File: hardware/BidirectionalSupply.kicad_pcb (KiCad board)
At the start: 4 copper layers, 132 x 107 mm, 190 parts, among them J1 USB-309GC-B-SU, J10 Conn_01x02, J11 Conn_01x08, J12 Conn_01x05, J13 Conn_01x02, J2 CON10, J3 CON2, J6 CON4, J7 CON2, J8 Conn_01x03, J9 Conn_01x12, Q1 SIR880BDP, Q10 SIR880BDP, Q11 SIR880BDP, Q12 SIR880BDP, Q2 SIR880BDP, Q3 SIR880BDP, Q4 SIR880BDP, Q5 SIR880BDP, Q6 SIR880BDP, Q7 SIR880BDP, Q8 SIR880BDP, Q9 SIR880BDP, SW1 SW_Push, SW2 SW_Push, U1 W25Q128JVS, U2 LM74810QDRRRQ1, U3 RP2350_60QFN, U4 BQ25758, U5 MAX17502EATB+T, U6 LM74810QDRRRQ1, U7 LM74810QDRRRQ1, U8 LM74810QDRRRQ1, Y1 ABM8-272-T3

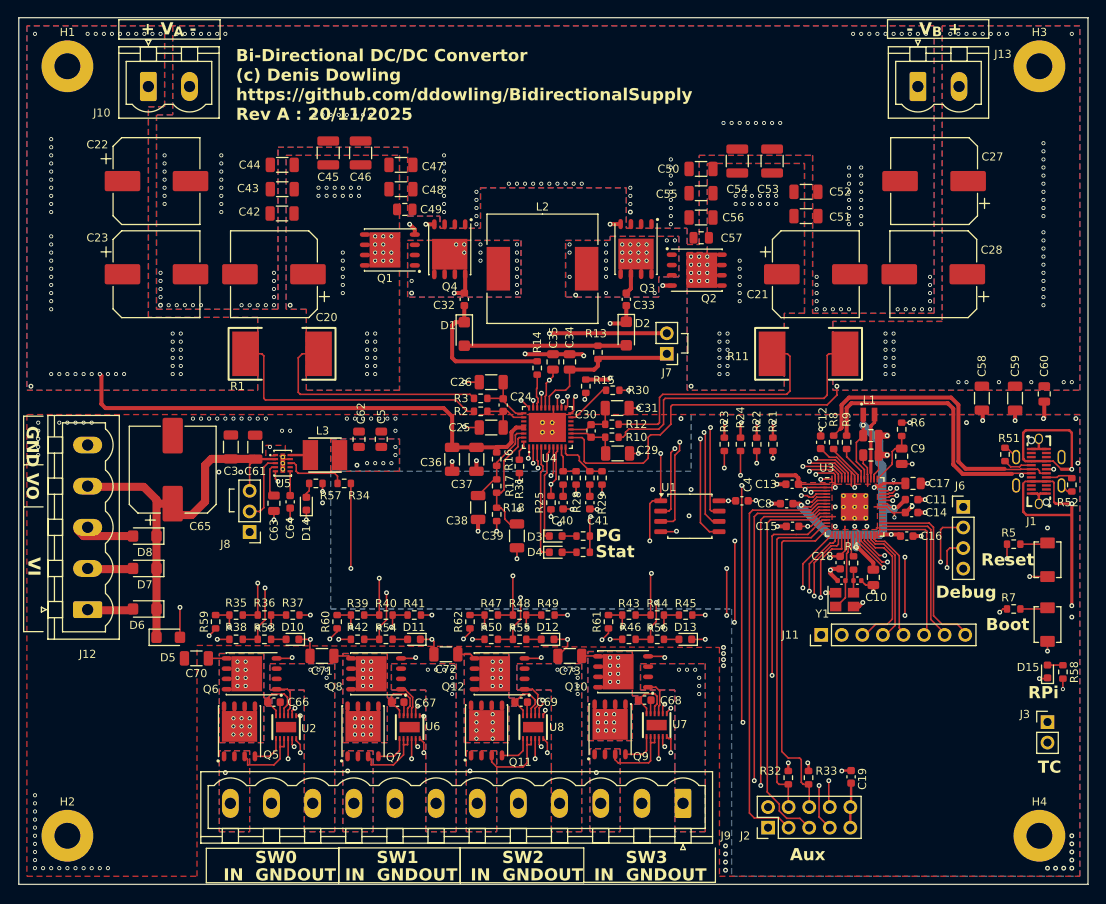
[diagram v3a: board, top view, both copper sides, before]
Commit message: * Added the JLCPCB Fabrication Plugin into KiCad and use this for the exports * Fixed problem detected with capacitor footprint for C42, C43, C44, C50, C51, C52
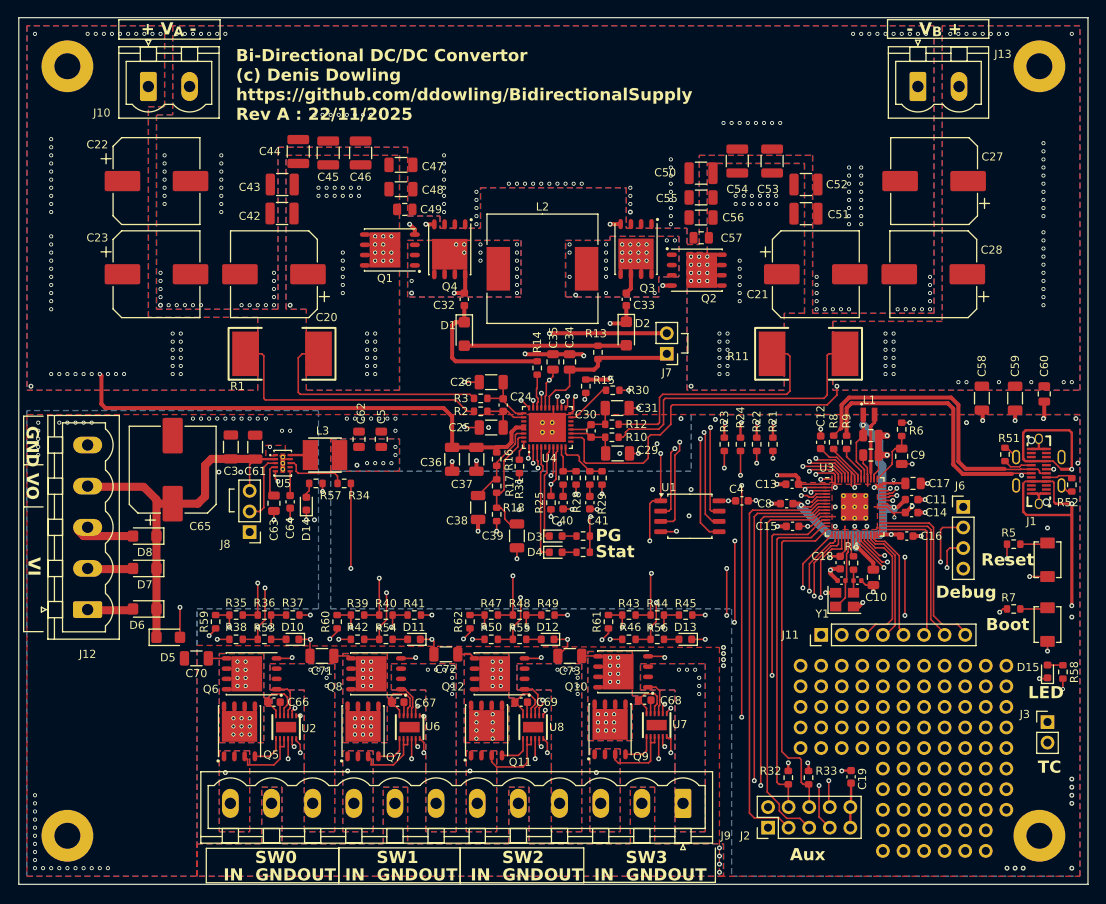
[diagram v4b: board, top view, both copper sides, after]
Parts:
- added REF**: Pad_D1.7mm_Drill1.0mm, BidirectionalSupply:Pad_D1.7mm_Drill1.0mm, F.Cu at (166.8, 132.6)
- added REF**: Pad_D1.7mm_Drill1.0mm, BidirectionalSupply:Pad_D1.7mm_Drill1.0mm, F.Cu at (151.6, 140.2)
- added REF**: Pad_D1.7mm_Drill1.0mm, BidirectionalSupply:Pad_D1.7mm_Drill1.0mm, F.Cu at (149.1, 140.2)
- added REF**: Pad_D1.7mm_Drill1.0mm, BidirectionalSupply:Pad_D1.7mm_Drill1.0mm, F.Cu at (171.9, 130.0)
- added REF**: Pad_D1.7mm_Drill1.0mm, BidirectionalSupply:Pad_D1.7mm_Drill1.0mm, F.Cu at (169.4, 132.6)
- added REF**: Pad_D1.7mm_Drill1.0mm, BidirectionalSupply:Pad_D1.7mm_Drill1.0mm, F.Cu at (156.7, 152.9)
- added REF**: Pad_D1.7mm_Drill1.0mm, BidirectionalSupply:Pad_D1.7mm_Drill1.0mm, F.Cu at (151.6, 132.6)
- added REF**: Pad_D1.7mm_Drill1.0mm, BidirectionalSupply:Pad_D1.7mm_Drill1.0mm, F.Cu at (156.7, 145.2)
- added REF**: Pad_D1.7mm_Drill1.0mm, BidirectionalSupply:Pad_D1.7mm_Drill1.0mm, F.Cu at (149.1, 132.6)
- added REF**: Pad_D1.7mm_Drill1.0mm, BidirectionalSupply:Pad_D1.7mm_Drill1.0mm, F.Cu at (161.8, 130.0)
- added REF**: Pad_D1.7mm_Drill1.0mm, BidirectionalSupply:Pad_D1.7mm_Drill1.0mm, F.Cu at (149.1, 130.0)
- added REF**: Pad_D1.7mm_Drill1.0mm, BidirectionalSupply:Pad_D1.7mm_Drill1.0mm, F.Cu at (166.8, 147.8)
- added REF**: Pad_D1.7mm_Drill1.0mm, BidirectionalSupply:Pad_D1.7mm_Drill1.0mm, F.Cu at (164.3, 132.6)
- added REF**: Pad_D1.7mm_Drill1.0mm, BidirectionalSupply:Pad_D1.7mm_Drill1.0mm, F.Cu at (146.5, 140.2)
- added REF**: Pad_D1.7mm_Drill1.0mm, BidirectionalSupply:Pad_D1.7mm_Drill1.0mm, F.Cu at (159.2, 135.1)
- added REF**: Pad_D1.7mm_Drill1.0mm, BidirectionalSupply:Pad_D1.7mm_Drill1.0mm, F.Cu at (166.8, 152.9)
- added REF**: Pad_D1.7mm_Drill1.0mm, BidirectionalSupply:Pad_D1.7mm_Drill1.0mm, F.Cu at (151.6, 130.0)
- added REF**: Pad_D1.7mm_Drill1.0mm, BidirectionalSupply:Pad_D1.7mm_Drill1.0mm, F.Cu at (169.4, 150.3)
- added REF**: Pad_D1.7mm_Drill1.0mm, BidirectionalSupply:Pad_D1.7mm_Drill1.0mm, F.Cu at (164.3, 150.3)
- added REF**: Pad_D1.7mm_Drill1.0mm, BidirectionalSupply:Pad_D1.7mm_Drill1.0mm, F.Cu at (159.2, 145.2)
- added REF**: Pad_D1.7mm_Drill1.0mm, BidirectionalSupply:Pad_D1.7mm_Drill1.0mm, F.Cu at (159.2, 132.6)
- added REF**: Pad_D1.7mm_Drill1.0mm, BidirectionalSupply:Pad_D1.7mm_Drill1.0mm, F.Cu at (154.1, 137.6)
- added REF**: Pad_D1.7mm_Drill1.0mm, BidirectionalSupply:Pad_D1.7mm_Drill1.0mm, F.Cu at (151.6, 135.1)
- added REF**: Pad_D1.7mm_Drill1.0mm, BidirectionalSupply:Pad_D1.7mm_Drill1.0mm, F.Cu at (169.4, 147.8)
- added REF**: Pad_D1.7mm_Drill1.0mm, BidirectionalSupply:Pad_D1.7mm_Drill1.0mm, F.Cu at (164.3, 137.6)
- added REF**: Pad_D1.7mm_Drill1.0mm, BidirectionalSupply:Pad_D1.7mm_Drill1.0mm, F.Cu at (159.2, 130.0)
- added REF**: Pad_D1.7mm_Drill1.0mm, BidirectionalSupply:Pad_D1.7mm_Drill1.0mm, F.Cu at (161.8, 132.6)
- added REF**: Pad_D1.7mm_Drill1.0mm, BidirectionalSupply:Pad_D1.7mm_Drill1.0mm, F.Cu at (156.7, 130.0)
- added REF**: Pad_D1.7mm_Drill1.0mm, BidirectionalSupply:Pad_D1.7mm_Drill1.0mm, F.Cu at (149.1, 137.6)
- added REF**: Pad_D1.7mm_Drill1.0mm, BidirectionalSupply:Pad_D1.7mm_Drill1.0mm, F.Cu at (171.9, 147.8)
- added REF**: Pad_D1.7mm_Drill1.0mm, BidirectionalSupply:Pad_D1.7mm_Drill1.0mm, F.Cu at (161.8, 135.1)
- added REF**: Pad_D1.7mm_Drill1.0mm, BidirectionalSupply:Pad_D1.7mm_Drill1.0mm, F.Cu at (171.9, 140.2)
- added REF**: Pad_D1.7mm_Drill1.0mm, BidirectionalSupply:Pad_D1.7mm_Drill1.0mm, F.Cu at (156.7, 142.7)
- added REF**: Pad_D1.7mm_Drill1.0mm, BidirectionalSupply:Pad_D1.7mm_Drill1.0mm, F.Cu at (161.8, 152.9)
- added REF**: Pad_D1.7mm_Drill1.0mm, BidirectionalSupply:Pad_D1.7mm_Drill1.0mm, F.Cu at (156.7, 140.2)
- added REF**: Pad_D1.7mm_Drill1.0mm, BidirectionalSupply:Pad_D1.7mm_Drill1.0mm, F.Cu at (164.3, 145.2)
- added REF**: Pad_D1.7mm_Drill1.0mm, BidirectionalSupply:Pad_D1.7mm_Drill1.0mm, F.Cu at (151.6, 137.6)
- added REF**: Pad_D1.7mm_Drill1.0mm, BidirectionalSupply:Pad_D1.7mm_Drill1.0mm, F.Cu at (159.2, 140.2)
- added REF**: Pad_D1.7mm_Drill1.0mm, BidirectionalSupply:Pad_D1.7mm_Drill1.0mm, F.Cu at (161.8, 140.2)
- added REF**: Pad_D1.7mm_Drill1.0mm, BidirectionalSupply:Pad_D1.7mm_Drill1.0mm, F.Cu at (166.8, 130.0)
- added REF**: Pad_D1.7mm_Drill1.0mm, BidirectionalSupply:Pad_D1.7mm_Drill1.0mm, F.Cu at (169.4, 140.2)
- added REF**: Pad_D1.7mm_Drill1.0mm, BidirectionalSupply:Pad_D1.7mm_Drill1.0mm, F.Cu at (161.8, 137.6)
- added REF**: Pad_D1.7mm_Drill1.0mm, BidirectionalSupply:Pad_D1.7mm_Drill1.0mm, F.Cu at (154.1, 130.0)
- added REF**: Pad_D1.7mm_Drill1.0mm, BidirectionalSupply:Pad_D1.7mm_Drill1.0mm, F.Cu at (171.9, 132.6)
- added REF**: Pad_D1.7mm_Drill1.0mm, BidirectionalSupply:Pad_D1.7mm_Drill1.0mm, F.Cu at (146.5, 130.0)
- added REF**: Pad_D1.7mm_Drill1.0mm, BidirectionalSupply:Pad_D1.7mm_Drill1.0mm, F.Cu at (169.4, 130.0)
- added REF**: Pad_D1.7mm_Drill1.0mm, BidirectionalSupply:Pad_D1.7mm_Drill1.0mm, F.Cu at (161.8, 142.7)
- added REF**: Pad_D1.7mm_Drill1.0mm, BidirectionalSupply:Pad_D1.7mm_Drill1.0mm, F.Cu at (159.2, 150.3)
- added REF**: Pad_D1.7mm_Drill1.0mm, BidirectionalSupply:Pad_D1.7mm_Drill1.0mm, F.Cu at (166.8, 135.1)
- added REF**: Pad_D1.7mm_Drill1.0mm, BidirectionalSupply:Pad_D1.7mm_Drill1.0mm, F.Cu at (146.5, 135.1)
- added REF**: Pad_D1.7mm_Drill1.0mm, BidirectionalSupply:Pad_D1.7mm_Drill1.0mm, F.Cu at (156.7, 135.1)
- added REF**: Pad_D1.7mm_Drill1.0mm, BidirectionalSupply:Pad_D1.7mm_Drill1.0mm, F.Cu at (171.9, 145.2)
- added REF**: Pad_D1.7mm_Drill1.0mm, BidirectionalSupply:Pad_D1.7mm_Drill1.0mm, F.Cu at (161.8, 150.3)
- added REF**: Pad_D1.7mm_Drill1.0mm, BidirectionalSupply:Pad_D1.7mm_Drill1.0mm, F.Cu at (166.8, 142.7)
- added REF**: Pad_D1.7mm_Drill1.0mm, BidirectionalSupply:Pad_D1.7mm_Drill1.0mm, F.Cu at (166.8, 150.3)
- added REF**: Pad_D1.7mm_Drill1.0mm, BidirectionalSupply:Pad_D1.7mm_Drill1.0mm, F.Cu at (149.1, 135.1)
- added REF**: Pad_D1.7mm_Drill1.0mm, BidirectionalSupply:Pad_D1.7mm_Drill1.0mm, F.Cu at (159.2, 137.6)
- added REF**: Pad_D1.7mm_Drill1.0mm, BidirectionalSupply:Pad_D1.7mm_Drill1.0mm, F.Cu at (166.8, 145.2)
- added REF**: Pad_D1.7mm_Drill1.0mm, BidirectionalSupply:Pad_D1.7mm_Drill1.0mm, F.Cu at (159.2, 142.7)
- added REF**: Pad_D1.7mm_Drill1.0mm, BidirectionalSupply:Pad_D1.7mm_Drill1.0mm, F.Cu at (164.3, 135.1)
- added REF**: Pad_D1.7mm_Drill1.0mm, BidirectionalSupply:Pad_D1.7mm_Drill1.0mm, F.Cu at (171.9, 137.6)
- added REF**: Pad_D1.7mm_Drill1.0mm, BidirectionalSupply:Pad_D1.7mm_Drill1.0mm, F.Cu at (164.3, 142.7)
- added REF**: Pad_D1.7mm_Drill1.0mm, BidirectionalSupply:Pad_D1.7mm_Drill1.0mm, F.Cu at (169.4, 137.6)
- added REF**: Pad_D1.7mm_Drill1.0mm, BidirectionalSupply:Pad_D1.7mm_Drill1.0mm, F.Cu at (169.4, 145.2)
- added REF**: Pad_D1.7mm_Drill1.0mm, BidirectionalSupply:Pad_D1.7mm_Drill1.0mm, F.Cu at (156.7, 137.6)
- added REF**: Pad_D1.7mm_Drill1.0mm, BidirectionalSupply:Pad_D1.7mm_Drill1.0mm, F.Cu at (164.3, 152.9)
- added REF**: Pad_D1.7mm_Drill1.0mm, BidirectionalSupply:Pad_D1.7mm_Drill1.0mm, F.Cu at (164.3, 130.0)
- added REF**: Pad_D1.7mm_Drill1.0mm, BidirectionalSupply:Pad_D1.7mm_Drill1.0mm, F.Cu at (169.4, 152.9)
- added REF**: Pad_D1.7mm_Drill1.0mm, BidirectionalSupply:Pad_D1.7mm_Drill1.0mm, F.Cu at (171.9, 142.7)
- added REF**: Pad_D1.7mm_Drill1.0mm, BidirectionalSupply:Pad_D1.7mm_Drill1.0mm, F.Cu at (169.4, 135.1)
- added REF**: Pad_D1.7mm_Drill1.0mm, BidirectionalSupply:Pad_D1.7mm_Drill1.0mm, F.Cu at (169.4, 142.7)
- added REF**: Pad_D1.7mm_Drill1.0mm, BidirectionalSupply:Pad_D1.7mm_Drill1.0mm, F.Cu at (159.2, 152.9)
- added REF**: Pad_D1.7mm_Drill1.0mm, BidirectionalSupply:Pad_D1.7mm_Drill1.0mm, F.Cu at (154.1, 140.2)
- added REF**: Pad_D1.7mm_Drill1.0mm, BidirectionalSupply:Pad_D1.7mm_Drill1.0mm, F.Cu at (164.3, 147.8)
- added REF**: Pad_D1.7mm_Drill1.0mm, BidirectionalSupply:Pad_D1.7mm_Drill1.0mm, F.Cu at (164.3, 140.2)
- added REF**: Pad_D1.7mm_Drill1.0mm, BidirectionalSupply:Pad_D1.7mm_Drill1.0mm, F.Cu at (161.8, 147.8)
- added REF**: Pad_D1.7mm_Drill1.0mm, BidirectionalSupply:Pad_D1.7mm_Drill1.0mm, F.Cu at (146.5, 132.6)
- added REF**: Pad_D1.7mm_Drill1.0mm, BidirectionalSupply:Pad_D1.7mm_Drill1.0mm, F.Cu at (156.7, 150.3)
- added REF**: Pad_D1.7mm_Drill1.0mm, BidirectionalSupply:Pad_D1.7mm_Drill1.0mm, F.Cu at (156.7, 132.6)
- added REF**: Pad_D1.7mm_Drill1.0mm, BidirectionalSupply:Pad_D1.7mm_Drill1.0mm, F.Cu at (154.1, 135.1)
- added REF**: Pad_D1.7mm_Drill1.0mm, BidirectionalSupply:Pad_D1.7mm_Drill1.0mm, F.Cu at (159.2, 147.8)
- added REF**: Pad_D1.7mm_Drill1.0mm, BidirectionalSupply:Pad_D1.7mm_Drill1.0mm, F.Cu at (154.1, 132.6)
- added REF**: Pad_D1.7mm_Drill1.0mm, BidirectionalSupply:Pad_D1.7mm_Drill1.0mm, F.Cu at (166.8, 140.2)
- added REF**: Pad_D1.7mm_Drill1.0mm, BidirectionalSupply:Pad_D1.7mm_Drill1.0mm, F.Cu at (171.9, 135.1)
- added REF**: Pad_D1.7mm_Drill1.0mm, BidirectionalSupply:Pad_D1.7mm_Drill1.0mm, F.Cu at (166.8, 137.6)
- added REF**: Pad_D1.7mm_Drill1.0mm, BidirectionalSupply:Pad_D1.7mm_Drill1.0mm, F.Cu at (146.5, 137.6)
- added REF**: Pad_D1.7mm_Drill1.0mm, BidirectionalSupply:Pad_D1.7mm_Drill1.0mm, F.Cu at (156.7, 147.8)
- added REF**: Pad_D1.7mm_Drill1.0mm, BidirectionalSupply:Pad_D1.7mm_Drill1.0mm, F.Cu at (161.8, 145.2)
- C42, C43, C44, C50, C51, C52: footprint Capacitor_SMD:C_1206_3216Metric -> Capacitor_SMD:C_1210_3225Metric
- moved C44 2.57 mm to (84.5, 66.5), turned to 90 degrees
- moved C52 0.90 mm to (147.2, 70.6)
- moved C43 0.58 mm to (82.5, 70.6)
- moved C50 0.53 mm to (134.2, 69.2)
- moved C55 0.53 mm to (134.2, 72.2)
- moved C51 0.30 mm to (147.2, 74.2)
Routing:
- net Net-(D5-K): track 51.3 -> 50.3 mm
- net Net-(J3-Pin_1): track 97.4 -> 96.6 mm
- net GND: vias 276 -> 280
- added copper zone on B.Cu, net (none)
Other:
- board text added: "Bi-Directional DC/DC Convertor (c) Denis Dowling https://github.com/ddowling/BidirectionalSupply Rev A : 22/11/2025"
- board text added: "LED"
- board text removed: "Bi-Directional DC/DC Convertor (c) Denis Dowling https://github.com/ddowling/BidirectionalSupply Rev A : 20/11/2025"
- board text removed: "RPi"
